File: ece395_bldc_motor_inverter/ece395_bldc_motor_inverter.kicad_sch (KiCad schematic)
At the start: 31 parts, among them J1 Conn_01x03_Socket, J2 Conn_01x05_Socket, Q1 CSD18540Q5B, Q10 CSD18540Q5B, Q2 CSD18540Q5B, Q3 CSD18540Q5B, Q4 CSD18540Q5B, Q5 CSD18540Q5B, Q6 CSD18540Q5B, Q7 CSD18540Q5B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

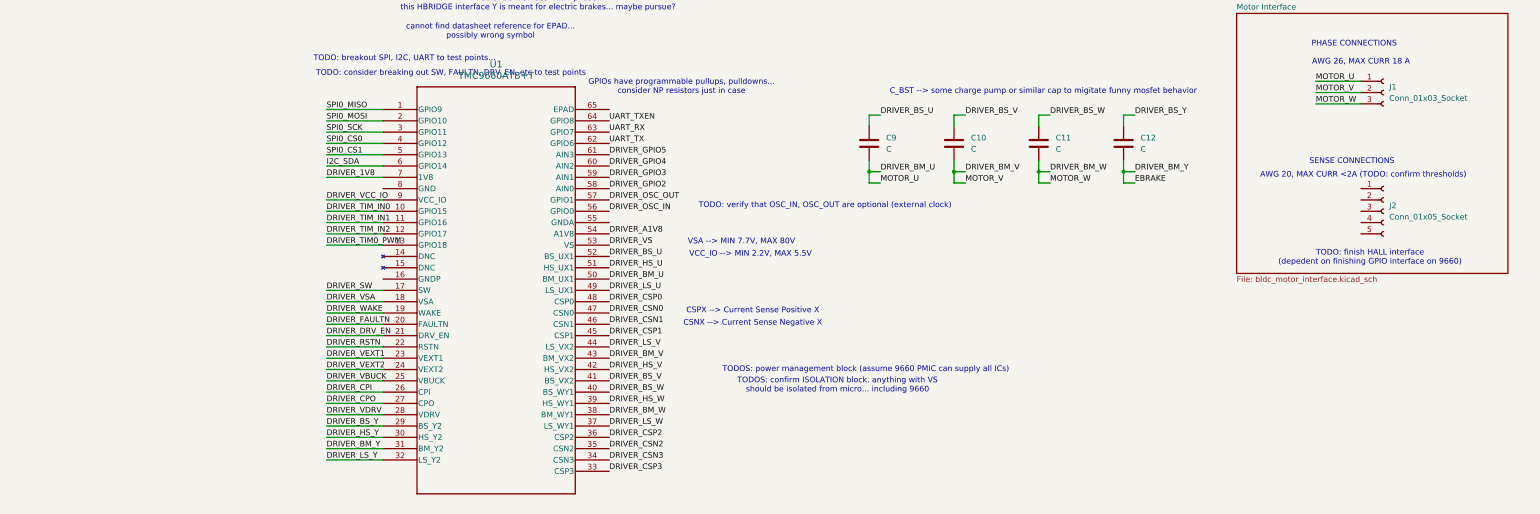
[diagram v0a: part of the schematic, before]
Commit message: added microcontroller
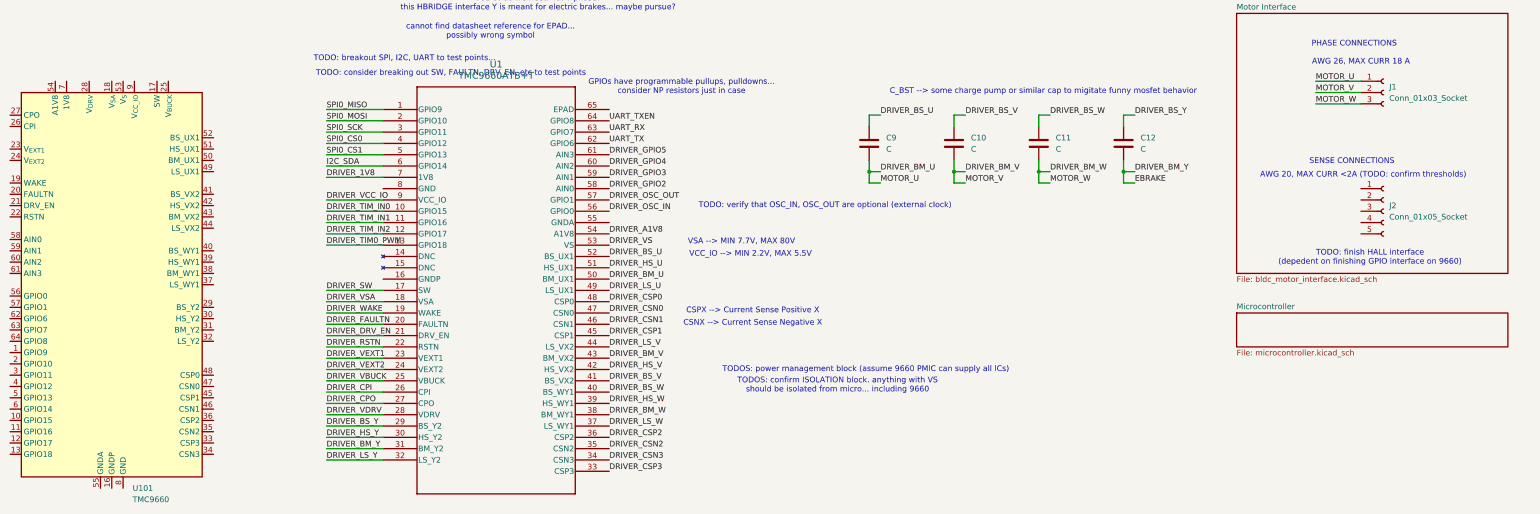
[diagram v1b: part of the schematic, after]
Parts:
- added U101: TMC9660, Package_DFN_QFN:QFN-64-1EP_9x9mm_P0.5mm_EP6x6mm_ThermalVias, symbol Driver_Motor_Analog:TMC9660
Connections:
- new net: U101.14 (DNC), U101.15 (DNC)
- new net: U101.65 (EP), U101.8 (GND)
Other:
- added sheet Microcontroller (microcontroller.kicad_sch)
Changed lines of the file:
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@@
+	)
+	(symbol
+		(lib_id "Driver_Motor_Analog:TMC9660")
+		(at -30.48 147.32 0)
+		(unit 1)
+		(exclude_from_sim no)
+		(in_bom yes)
+		(on_board yes)
+		(dnp no)
+		(fields_autoplaced yes)
+		(property "Reference" "U101"
+			(at -25.7967 193.04 0)
+			(effects
+				(font
+					(size 1.27 1.27)
+				)
+				(justify left)
+			)
+		)
+		(property "Value" "TMC9660"
+			(at -25.7967 195.58 0)
+			(effects
+				(font
+					(size 1.27 1.27)
+				)
+				(justify left)
+			)
+		)
+		(property "Footprint" "Package_DFN_QFN:QFN-64-1EP_9x9mm_P0.5mm_EP6x6mm_ThermalVias"
+			(at -30.48 208.28 0)
+			(effects
+				(font
+					(size 1.27 1.27)
+				)
+				(hide yes)
+			)
+		)
+		(property "Datasheet" "https://www.analog.com/media/en/technical-documentation/data-sheets/tmc9660.pdf"
+			(at -30.48 208.28 0)
+			(effects
+				(font
+					(size 1.27 1.27)
+				)
+				(hide yes)
+			)
+		)
+		(property "Description" "70V Smart Gate Driver with Servo (FOC) Controller in HW and Buck Converter, TQFN-64"
+			(at -30.48 208.28 0)
+			(effects
+				(font
+					(size 1.27 1.27)
+				)
+				(hide yes)
+			)
+		)
+		(pin "64"
+		)
+		(pin "4"
+		)
+		(pin "19"
+		)
+		(pin "63"
+		)
+		(pin "22"
+		)
+		(pin "58"
+		)
+		(pin "27"
+		)
+		(pin "23"
+		)
+		(pin "20"
+		)
+		(pin "21"
+		)
+		(pin "61"
+		)
+		(pin "56"
+		)
+		(pin "3"
+		)
+		(pin "16"
+		)
+		(pin "55"
+		)
+		(pin "11"
+		)
+		(pin "26"
+		)
+		(pin "24"
+		)
+		(pin "59"
+		)
+		(pin "60"
+		)
+		(pin "62"
+		)
+		(pin "57"
+		)
+		(pin "1"
+		)
+		(pin "2"
+		)
+		(pin "5"
+		)
+		(pin "6"
+		)
+		(pin "10"
+		)
+		(pin "13"
+		)
+		(pin "28"
+		)
+		(pin "32"
+		)
+		(pin "12"
+		)
+		(pin "9"
+		)
+		(pin "7"
+		)
+		(pin "17"
+		)
+		(pin "54"
+		)
+		(pin "44"
+		)
+		(pin "18"
+		)
+		(pin "43"
+		)
+		(pin "42"
+		)
+		(pin "52"
+		)
+		(pin "39"
+		)
+		(pin "53"
+		)
+		(pin "8"
+		)
+		(pin "40"
+		)
+		(pin "37"
+		)
+		(pin "50"
+		)
+		(pin "51"
+		)
+		(pin "49"
+		)
+		(pin "29"
+		)
+		(pin "31"
+		)
+		(pin "41"
+		)
+		(pin "25"
+		)
+		(pin "38"
+		)
+		(pin "30"
+		)
+		(pin "48"
+		)
+		(pin "45"
+		)
+		(pin "47"
+		)
+		(pin "46"
+		)
+		(pin "36"
+		)
+		(pin "35"
+		)
+		(pin "33"
+		)
+		(pin "14"
+		)
+		(pin "15"
+		)
+		(pin "34"
+		)
+		(pin "65"
+		)
+		(instances
+			(project ""
+				(path "/f8816ca8-d12a-4d6e-83e4-586d8ea9408b"
+					(reference "U101")
+					(unit 1)
+				)
+			)
+		)
 	)
 	(symbol
@@
 				)
 			)
+		)
+	)
+	(sheet
+		(at 222.25 153.67)
+		(size 60.96 7.62)
+		(exclude_from_sim no)
+		(in_bom yes)
+		(on_board yes)
+		(dnp no)
+		(fields_autoplaced yes)
+		(stroke
+			(width 0.1524)
+			(type solid)
+		)
+		(fill
+			(color 0 0 0 0.0000)
+		)
+		(property "Sheetname" "Microcontroller"
+			(at 222.25 152.9584 0)
+			(effects
+				(font
+					(size 1.27 1.27)
+				)
+				(justify left bottom)
+			)
+		)
+		(property "Sheetfile" "microcontroller.kicad_sch"
+			(at 222.25 161.8746 0)
+			(effects
+				(font
+					(size 1.27 1.27)
+				)
+				(justify left top)
+			)
+		)
+		(instances
+			(project "ece395_bldc_motor_inverter"
+				(path "/f8816ca8-d12a-4d6e-83e4-586d8ea9408b"
+					(page "4")
+				)
+			)

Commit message: tmc9660 libraries
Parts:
- U101: footprint Package_DFN_QFN:QFN-64-1EP_9x9mm_P0.5mm_EP6x6mm_ThermalVias -> Package_QFN:QFN-64-1EP_9x9mm_P0.5mm_EP6.3x6.3mm
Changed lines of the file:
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@@
 			)
 		)
-		(property "Footprint" "Package_DFN_QFN:QFN-64-1EP_9x9mm_P0.5mm_EP6x6mm_ThermalVias"
+		(property "Footprint" "Package_QFN:QFN-64-1EP_9x9mm_P0.5mm_EP6.3x6.3mm"
 			(at -30.48 208.28 0)
 			(effects

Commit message: switched out tmc9660 symbol
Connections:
- net DRIVER_VCC_IO is gone; now on net +3V3: C6.1, U1.9 (VCC_IO)
- net DRIVER_1V8: no longer C4.1
- net DRIVER_A1V8: now also U101.54 (A1V8)
- net DRIVER_BM_U: now also U101.50 (BM_UX1)
- net DRIVER_BM_V: now also U101.43 (BM_VX2)
- net DRIVER_BM_W: now also U101.38 (BM_WY1)
- net DRIVER_BM_Y: now also U101.31 (BM_Y2)
- net DRIVER_BS_U: now also U101.52 (BS_UX1)
- net DRIVER_BS_V: now also U101.41 (BS_VX2)
- net DRIVER_BS_W: now also U101.40 (BS_WY1)
- net DRIVER_BS_Y: now also U101.29 (BS_Y2)
- net DRIVER_CPI: now also U101.27 (CPO)
- net DRIVER_CPO: now also U101.26 (CPI)
- net DRIVER_CSN0: now also U101.47 (CSN0)
- net DRIVER_CSN1: now also U101.46 (CSN1)
- net DRIVER_CSN2: now also U101.35 (CSN2)
- net DRIVER_CSN3: now also U101.34 (CSN3)
- net DRIVER_CSP0: now also U101.48 (CSP0)
- net DRIVER_CSP1: now also U101.45 (CSP1)
- net DRIVER_CSP2: now also U101.36 (CSP2)
- net DRIVER_CSP3: now also U101.33 (CSP3)
- net DRIVER_DRV_EN: now also U101.21 (DRV_EN)
- net DRIVER_FAULTN: now also U101.20 (FAULTN)
- net DRIVER_GPIO2: now also U101.58 (AIN0)
- net DRIVER_GPIO3: now also U101.59 (AIN1)
- net DRIVER_GPIO4: now also U101.60 (AIN2)
- net DRIVER_GPIO5: now also U101.61 (AIN3)
- net DRIVER_HS_U: now also U101.51 (HS_UX1)
- net DRIVER_HS_V: now also U101.42 (HS_VX2)
- net DRIVER_HS_W: now also U101.39 (HS_WY1)
- net DRIVER_HS_Y: now also U101.30 (HS_Y2)
- net DRIVER_LS_U: now also U101.49 (LS_UX1)
- net DRIVER_LS_V: now also U101.44 (LS_VX2)
- net DRIVER_LS_W: now also U101.37 (LS_WY1)
- net DRIVER_LS_Y: now also U101.32 (LS_Y2)
- net DRIVER_OSC_IN: now also U101.56 (GPIO0)
- net DRIVER_OSC_OUT: now also U101.57 (GPIO1)
- net DRIVER_RSTN: now also U101.22 (RSTN)
- net DRIVER_SW: now also U101.17 (SW)
- net DRIVER_TIM0_PWM: now also U101.13 (GPIO18)
- net DRIVER_TIM_IN0: now also U101.10 (GPIO15)
- net DRIVER_TIM_IN1: now also U101.11 (GPIO16)
- net DRIVER_TIM_IN2: now also U101.12 (GPIO17)
- net DRIVER_VBUCK: no longer C1.1, L1.2
- net DRIVER_VDRV: now also U101.28 (V_{DRV})
- net DRIVER_VEXT1: no longer C2.1
- net DRIVER_VEXT2: no longer C3.1
- net DRIVER_WAKE: now also U101.19 (WAKE)
- net GND: now also U101.16 (GNDP), U101.55 (GNDA), U101.65 (EP), U101.8 (GND)
- net I2C_SDA: now also U101.6 (GPIO14)
- net SPI0_CS0: now also U101.4 (GPIO12)
- net SPI0_CS1: now also U101.5 (GPIO13)
- net SPI0_MISO: now also U101.1 (GPIO9)
- net SPI0_MOSI: now also U101.2 (GPIO10)
- net SPI0_SCK: now also U101.3 (GPIO11)
- net UART_RX: now also U101.63 (GPIO7)
- net UART_TX: now also U101.62 (GPIO6)
- net UART_TXEN: now also U101.64 (GPIO8)
- net VBATT: now reaches U101.18 (V_{SA})
- net VBATT: now also U101.53 (V_{S})
- net DRIVER_V_{EXT1}: now reaches U101.23 (V_{EXT1})
- net DRIVER_V_{EXT1}: now also C2.1
- net DRIVER_V_{EXT2}: now reaches U101.24 (V_{EXT2})
- net DRIVER_V_{EXT2}: now also C3.1
- net DRIVER_V_{BUCK}: now reaches U101.25 (V_{BUCK})
- net DRIVER_V_{BUCK}: now also C1.1, L1.2
- net +1V8: now reaches U101.7 (1V8)
- net +1V8: now also C4.1
- net +3V3: now reaches U101.9 (V_{CC_IO})
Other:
- note removed: "cannot find datasheet reference for EPAD... possibly wrong symbol"
- company: (none) -> University of Illinois Urbana-Champaign
- title: (none) -> BLDC Motor Inverter
- moved on the sheet: U1, U101
